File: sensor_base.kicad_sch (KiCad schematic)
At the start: 28 parts, among them J14 Calibration_In, J2 PT-100_TEMP_IN, J5 SPARE, U11 OPA2397DGKR, U17 DHT20, U3 ESDA5V3SC5

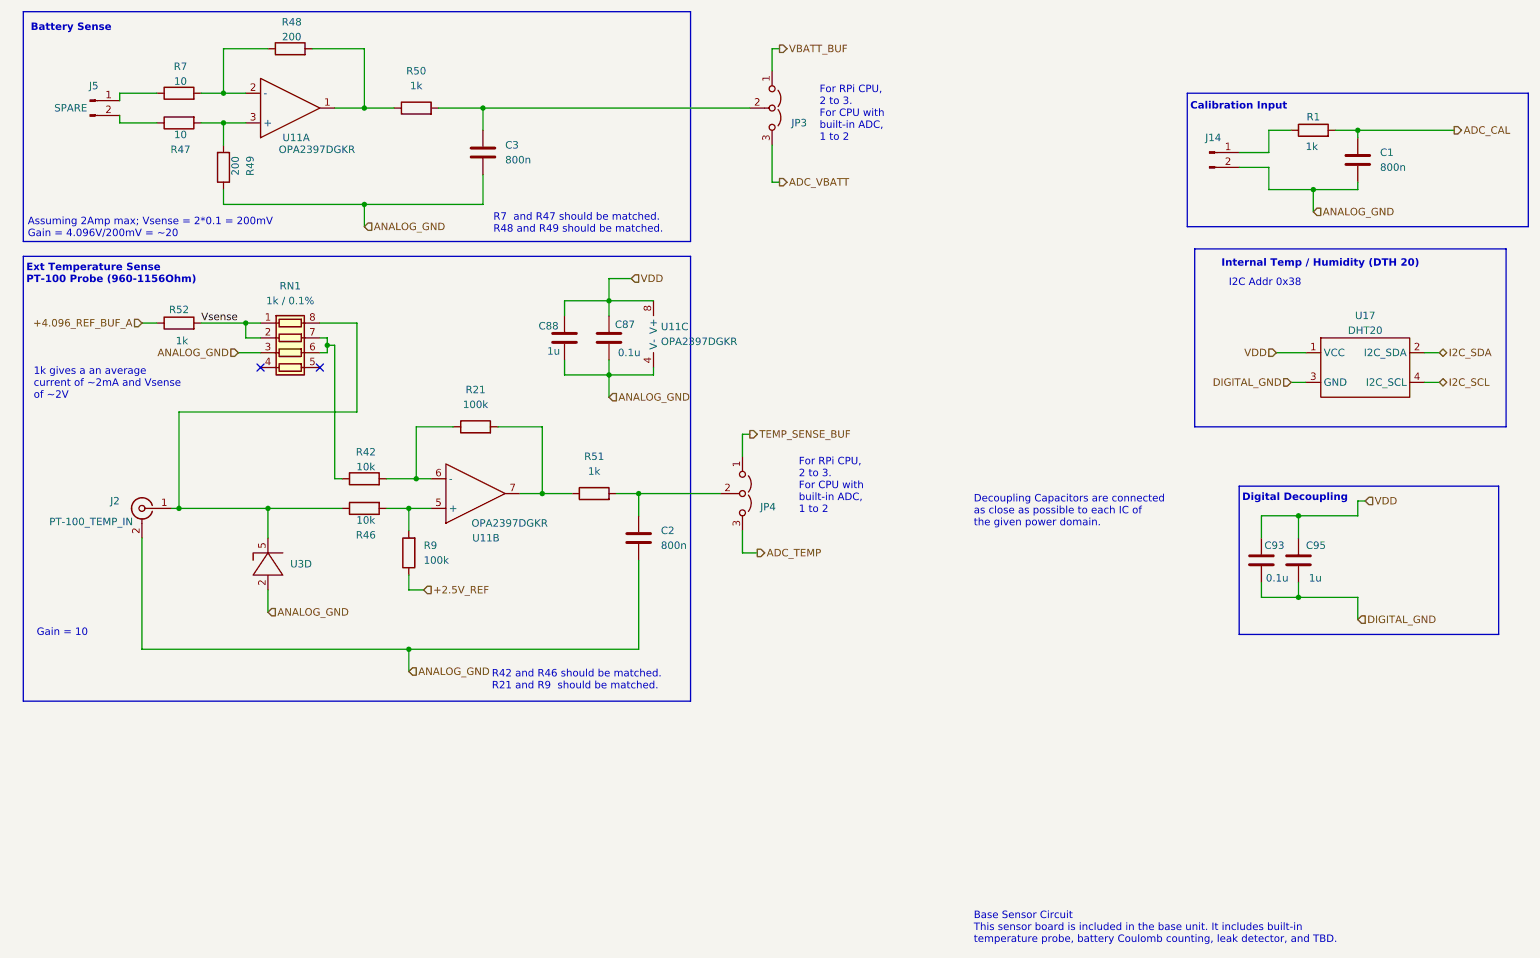
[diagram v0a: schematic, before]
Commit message: Prototype v0.3.1 WIP Just a maintenance checkin. Many changes - Removed the Base Sensor schematic and put all sensors into SensorPrototype - Added a constant current LED driver for camera illumination - Added a 12V buck converter to the input in support of external power - Added a low-side current sense to the input - Added an LDO regulator to cleanup Buck output and to provide battery regulation - Added support for an internal battery + switchover / charge circuit. - Swapped headers for proper board connectors - Added an RS485 transceiver for external + modem communication - Added an additional temperature circuit in support of NTC probes - Incorporated the AS Dissolved Oxygen sensor into the main board - Added DC return path resistors to non-inverting amps - Fixed mixed power domain bug - Moved AS isolated carrier board to 3.3V rail and routed the shutdown pin to en/sh - Moved the DHT20 to the 3.3V rail - In the process of re-routing ADC channels.
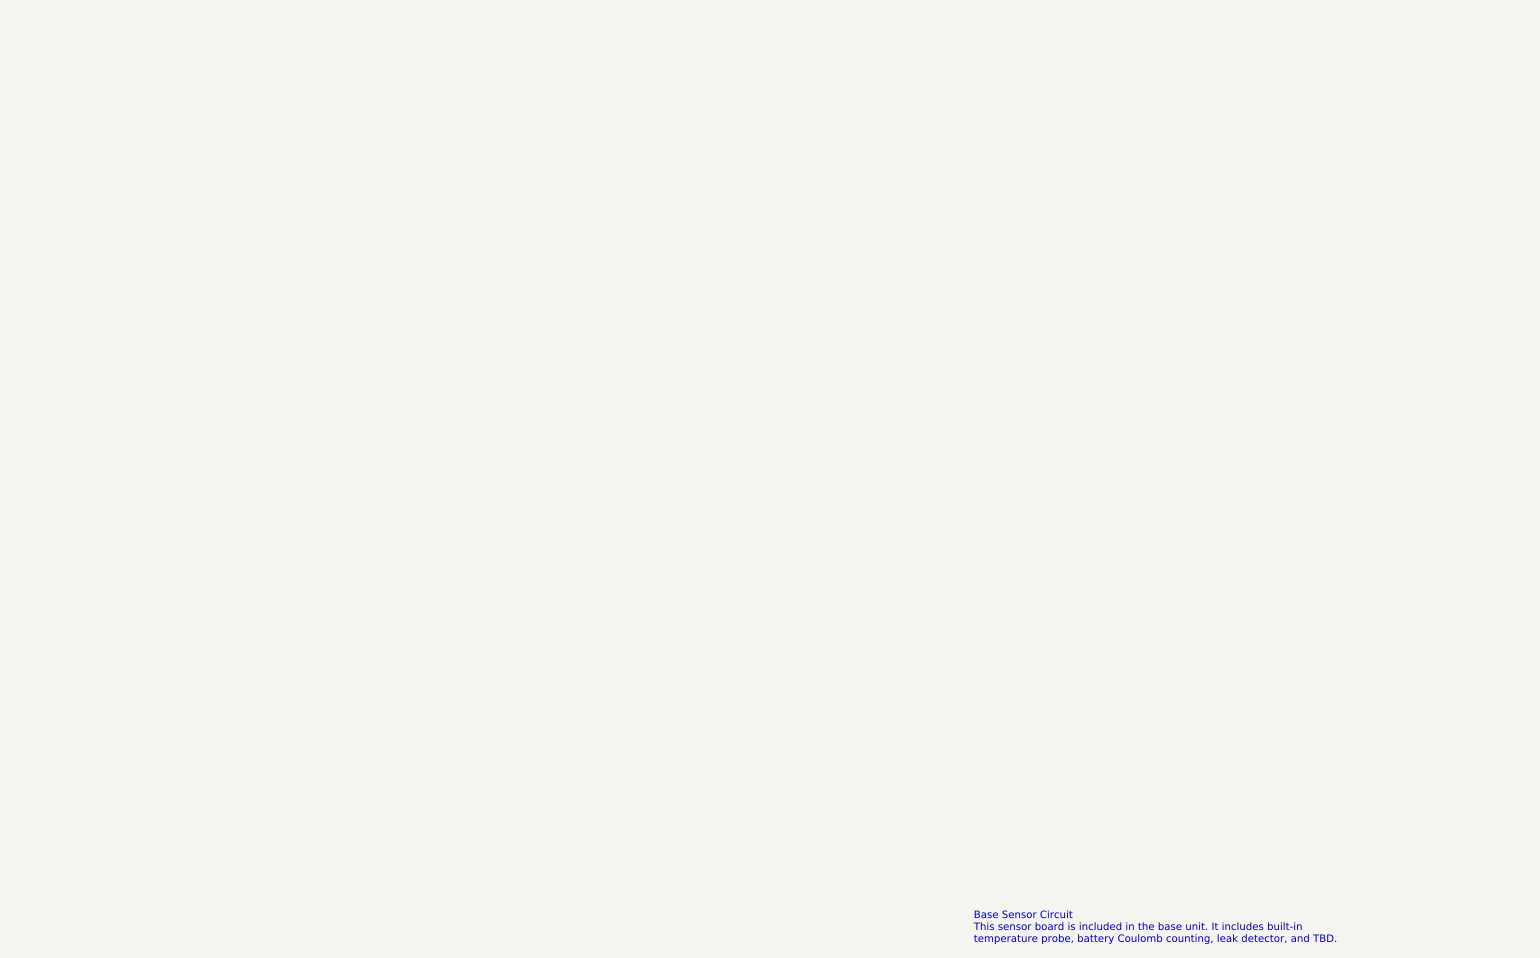
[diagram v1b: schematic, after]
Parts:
- removed C1, C2, C3: 800n, Capacitor_SMD:C_1210_3225Metric_Pad1.33x2.70mm_HandSolder, symbol Device:C
- removed C87, C93: 0.1u, Capacitor_SMD:C_1210_3225Metric_Pad1.33x2.70mm_HandSolder, symbol Device:C
- removed C88, C95: 1u, Capacitor_SMD:C_1210_3225Metric_Pad1.33x2.70mm_HandSolder, symbol Device:C
- removed J14: Calibration_In, Connector_PinHeader_2.54mm:PinHeader_1x02_P2.54mm_Vertical_SMD_Pin1Left, symbol Connector:Conn_01x02_Pin
- removed J2: PT-100_TEMP_IN, Connector_PinHeader_2.54mm:PinHeader_1x02_P2.54mm_Vertical_SMD_Pin1Left, symbol Connector:Conn_Coaxial
- removed J5: SPARE, Connector_PinHeader_2.54mm:PinHeader_1x02_P2.54mm_Vertical_SMD_Pin1Left, symbol Connector:Conn_01x02_Pin
- removed JP3: RPi_Batt, Connector_PinHeader_2.54mm:PinHeader_1x03_P2.54mm_Vertical_SMD_Pin1Left, symbol Jumper:Jumper_3_Open
- removed JP4: RPi_Temp, Connector_PinHeader_2.54mm:PinHeader_1x03_P2.54mm_Vertical_SMD_Pin1Left, symbol Jumper:Jumper_3_Open
- removed R1, R50, R51, R52: 1k, Resistor_SMD:R_1210_3225Metric_Pad1.30x2.65mm_HandSolder, symbol Device:R
- removed R21, R9: 100k, Resistor_SMD:R_1210_3225Metric_Pad1.30x2.65mm_HandSolder, symbol Device:R
- removed R42, R46: 10k, Resistor_SMD:R_1210_3225Metric_Pad1.30x2.65mm_HandSolder, symbol Device:R
- removed R47, R7: 10, Resistor_SMD:R_1210_3225Metric_Pad1.30x2.65mm_HandSolder, symbol Device:R
- removed R48, R49: 200, Resistor_SMD:R_1210_3225Metric_Pad1.30x2.65mm_HandSolder, symbol Device:R
- removed RN1: 1k / 0.1%, Resistor_SMD:R_Array_Concave_4x0603, symbol Device:R_Pack04
- removed U11: OPA2397DGKR, Package_SO:SOIC-8_3.9x4.9mm_P1.27mm, symbol Op-Amp-Extended:OPA2397DR
- removed U17: DHT20, Connector_PinSocket_2.54mm:PinSocket_1x04_P2.54mm_Vertical_SMD_Pin1Left, symbol AndrewAdditions:DHT20
- removed U3: ESDA5V3SC5, Package_TO_SOT_SMD:SOT-23-5, symbol AndrewAdditions:sda5v3sc6_split
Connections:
- no-connect marks 2 -> 0
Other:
- note removed: "1k gives a an average current of ~2mA and Vsense of ~2V"
- note removed: "Assuming 2Amp max; Vsense = 2*0.1 = 200mV Gain = 4.096V/200mV = ~20"
- note removed: "Battery Sense"
- note removed: "Calibration Input"
- note removed: "Decoupling Capacitors are connected as close as possible to each IC of the given power domain."
- note removed: "Digital Decoupling"
- note removed: "Ext Temperature Sense PT-100 Probe (960-1156Ohm)"
- note removed: "For RPi CPU, 2 to 3. For CPU with built-in ADC, 1 to 2"
- note removed: "Gain = 10"
- note removed: "I2C Addr 0x38"
- note removed: "Internal Temp / Humidity (DTH 20)"
- note removed: "R42 and R46 should be matched. R21 and R9 should be matched."
- note removed: "R7 and R47 should be matched. R48 and R49 should be matched."
